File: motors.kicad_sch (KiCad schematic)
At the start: 15 parts, among them J5 left_motor_connector, J6 right_motor_connector, U2 L293D

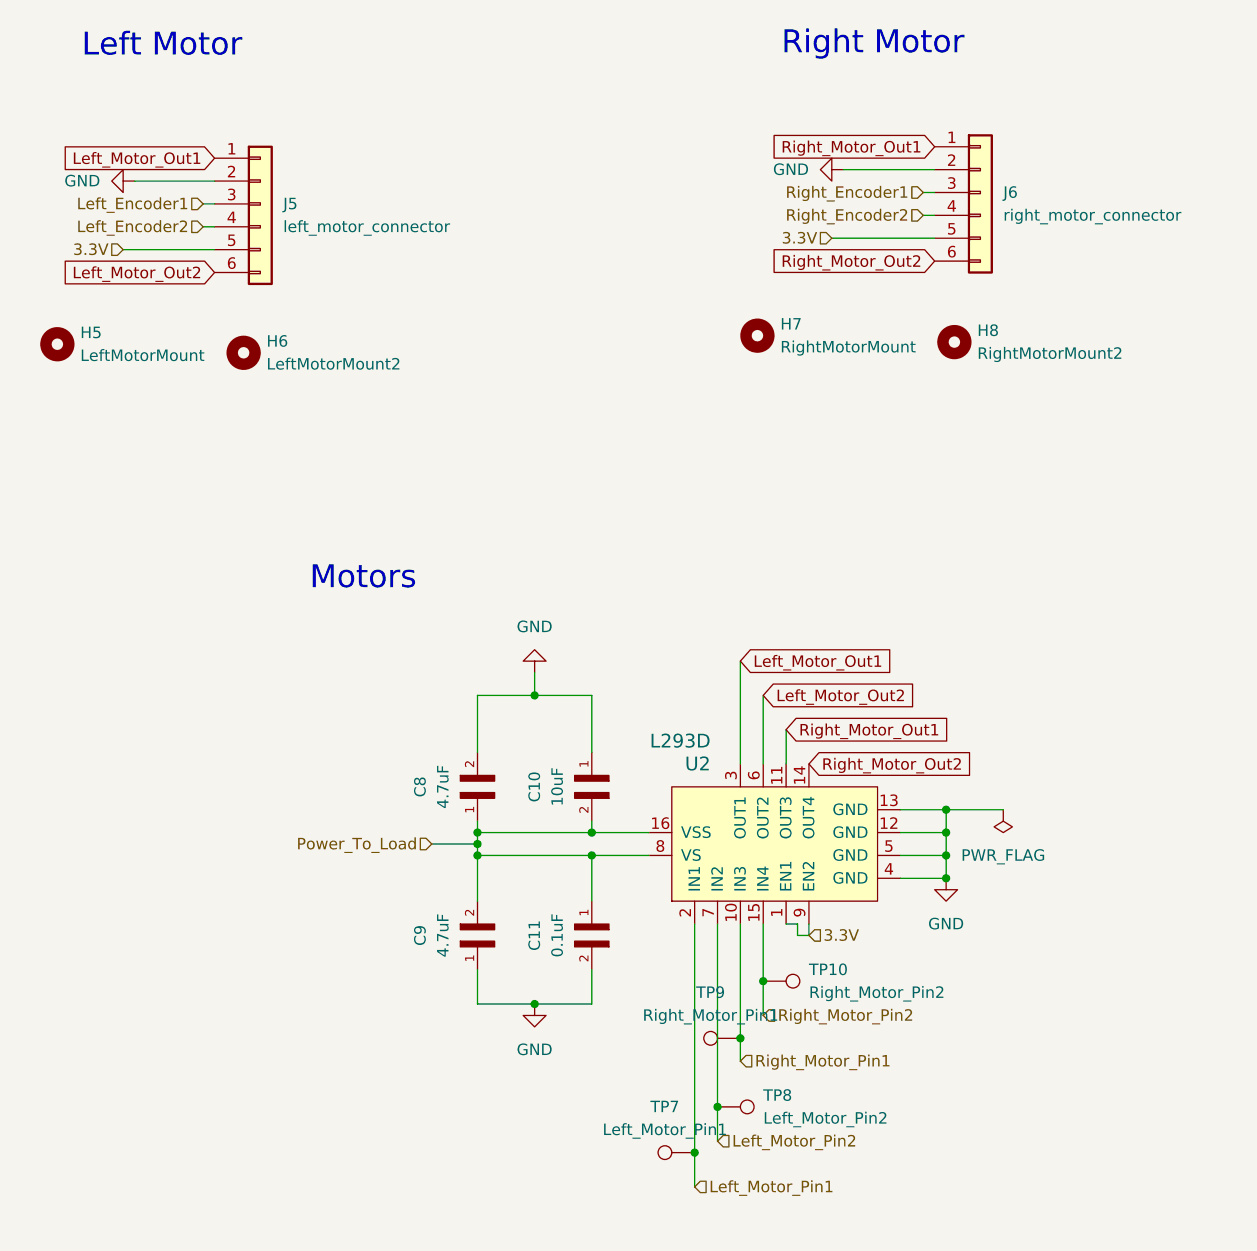
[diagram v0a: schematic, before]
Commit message: schematic: all errors and warnings gone
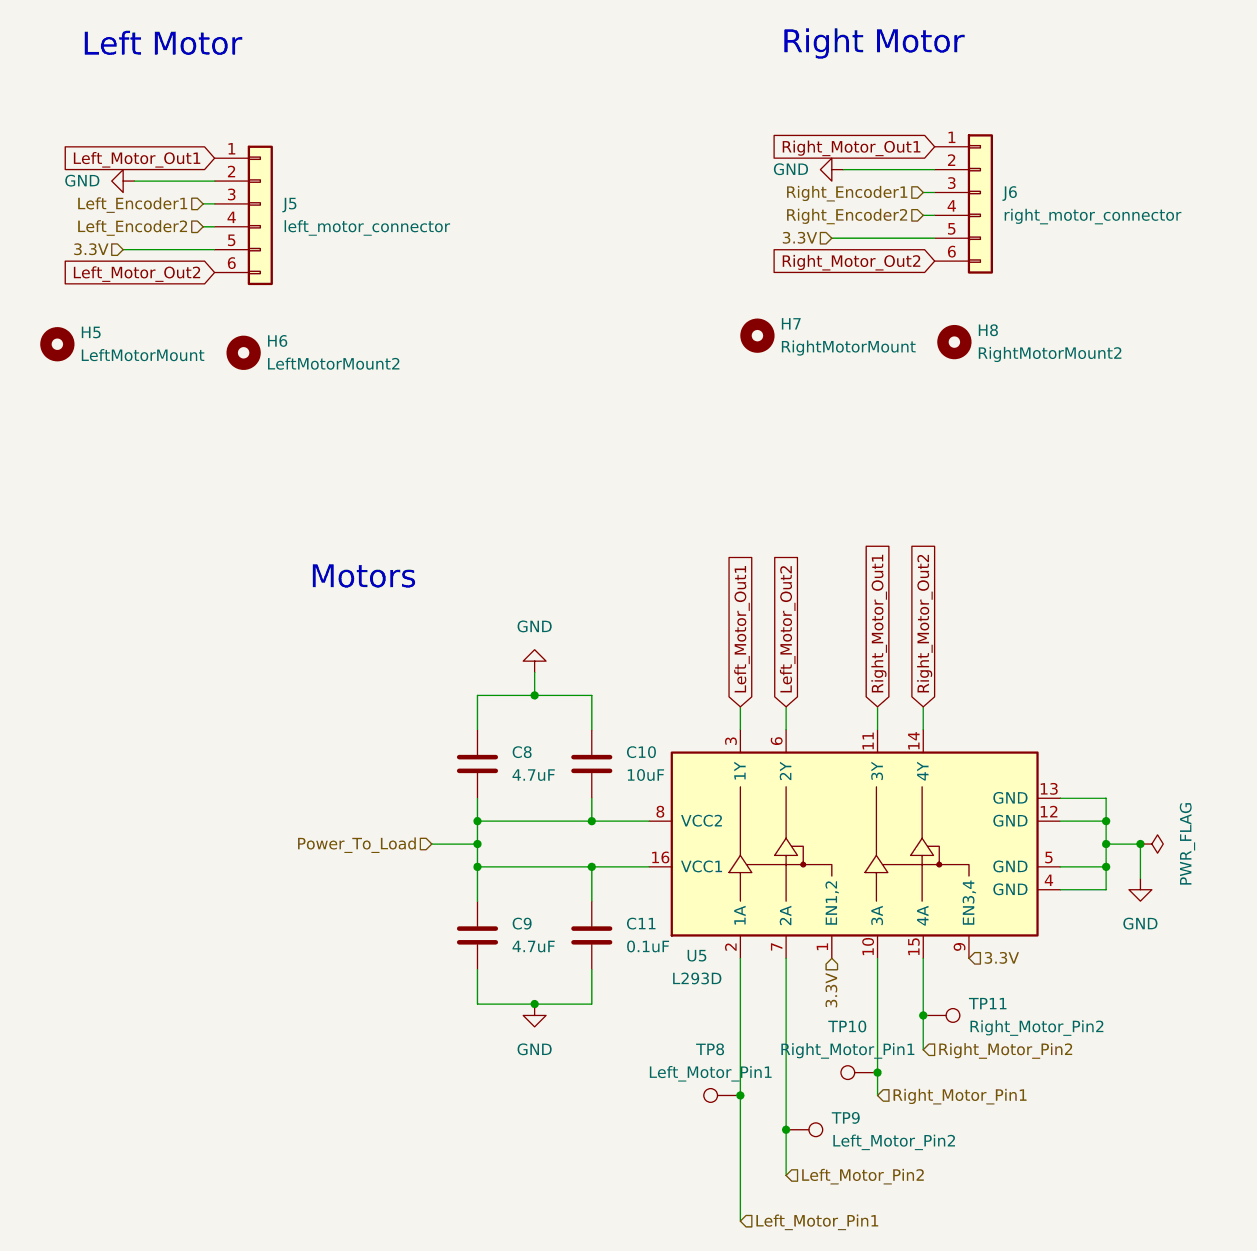
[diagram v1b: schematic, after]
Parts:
- removed C10: 10uF, Capacitor_SMD:C_0805_2012Metric_Pad1.18x1.45mm_HandSolder, symbol CL10A106KP8NNNC:CL10A106KP8NNNC
- removed C11: 0.1uF, Capacitor_SMD:C_0805_2012Metric_Pad1.18x1.45mm_HandSolder, symbol CL05B104KO5NNNC:CL05B104KO5NNNC
- removed C8, C9: 4.7uF, Capacitor_SMD:C_0805_2012Metric_Pad1.18x1.45mm_HandSolder, symbol CL10A475KO8NNNC:CL10A475KO8NNNC
- removed TP7: Left_Motor_Pin1, TestPoint:TestPoint_THTPad_2.0x2.0mm_Drill1.0mm, symbol Connector:TestPoint
- removed U2: L293D, Package_DIP:DIP-16_W7.62mm_Socket, symbol Robotastisch:L293D
- added C10: 10uF, Capacitor_SMD:C_0805_2012Metric_Pad1.18x1.45mm_HandSolder, symbol Device:C
- added C11: 0.1uF, Capacitor_SMD:C_0805_2012Metric_Pad1.18x1.45mm_HandSolder, symbol Device:C
- added C8, C9: 4.7uF, Capacitor_SMD:C_0805_2012Metric_Pad1.18x1.45mm_HandSolder, symbol Device:C
- added TP11: Right_Motor_Pin2, TestPoint:TestPoint_THTPad_2.0x2.0mm_Drill1.0mm, symbol Connector:TestPoint
- added U5: L293D, Package_DIP:DIP-16_W7.62mm, symbol Driver_Motor:L293D
- TP10: value Right_Motor_Pin2 -> Right_Motor_Pin1
- TP8: value Left_Motor_Pin2 -> Left_Motor_Pin1
- TP9: value Right_Motor_Pin1 -> Left_Motor_Pin2
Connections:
- net 3.3V: now also U5.1 (EN1,2), U5.9 (EN3,4)
- net GND: now also C10.1, C11.2, C8.1, C9.2, U5.12 (GND), U5.13 (GND), U5.4 (GND), U5.5 (GND)
- net Left_Motor_Out1: now also U5.3 (1Y)
- net Left_Motor_Out2: now also U5.6 (2Y)
- net Left_Motor_Pin1: now also TP8.1, U5.2 (1A)
- net Left_Motor_Pin2: now also TP9.1, U5.7 (2A); no longer TP8.1
- net Power_To_Load: now also C10.2, C11.1, C8.2, C9.1, U5.16 (VCC1), U5.8 (VCC2)
- net Right_Motor_Out1: now also U5.11 (3Y)
- net Right_Motor_Out2: now also U5.14 (4Y)
- net Right_Motor_Pin1: now also TP10.1, U5.10 (3A); no longer TP9.1
- net Right_Motor_Pin2: now also TP11.1, U5.15 (4A); no longer TP10.1

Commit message: pcb: all wired up, most warnings can't be fixed.
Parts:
- LM1: renamed from TP8; value Left_Motor_Pin1 -> Testpoint
- LM2: renamed from TP9; value Left_Motor_Pin2 -> Testpoint
- RM1: renamed from TP10; value Right_Motor_Pin1 -> Testpoint
- RM2: renamed from TP11; value Right_Motor_Pin2 -> Testpoint
- renumbered U5 to U2
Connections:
- net GND: now also C10.2, C8.2; no longer C10.1, C8.1
- net Power_To_Load: now also C10.1, C8.1; no longer C10.2, C8.2
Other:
- moved on the sheet: C10, C8
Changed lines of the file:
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@@
 		(dnp no)
 		(fields_autoplaced yes)
-		(property "Reference" "TP10"
+		(property "Reference" "RM1"
 			(at 117.348 140.97 90)
 			(effects
@@
 			)
 		)
-		(property "Value" "Right_Motor_Pin1"
+		(property "Value" "Testpoint"
 			(at 117.348 143.51 90)
 			(effects
@@
 			(project "RoboMaus"
 				(path "/0ec4df52-ef34-4d49-9154-02bae5c96110/599bc449-1c79-4d43-aa66-86532ca36330"
-					(reference "TP10")
+					(reference "RM1")
 					(unit 1)
 				)
@@
 	(symbol
 		(lib_id "Device:C")
-		(at 88.9 111.76 0)
+		(at 88.9 111.76 180)
 		(unit 1)
 		(exclude_from_sim no)
@@
 					(size 1.27 1.27)
 				)
-				(justify left)
+				(justify right)
 			)
 		)
@@
 					(size 1.27 1.27)
 				)
-				(justify left)
+				(justify right)
 			)
 		)
 		(property "Footprint" "Capacitor_SMD:C_0805_2012Metric_Pad1.18x1.45mm_HandSolder"
-			(at 89.8652 115.57 0)
+			(at 87.9348 107.95 0)
 			(effects
 				(font
@@
 		(dnp no)
 		(fields_autoplaced yes)
-		(property "Reference" "TP9"
+		(property "Reference" "LM2"
 			(at 115.57 151.1299 90)
 			(effects
@@
 			)
 		)
-		(property "Value" "Left_Motor_Pin2"
+		(property "Value" "Testpoint"
 			(at 115.57 153.6699 90)
 			(effects
@@
 			(project "RoboMaus"
 				(path "/0ec4df52-ef34-4d49-9154-02bae5c96110/599bc449-1c79-4d43-aa66-86532ca36330"
-					(reference "TP9")
+					(reference "LM2")
 					(unit 1)
 				)
@@
 	(symbol
 		(lib_id "Device:C")
-		(at 76.2 111.76 0)
+		(at 76.2 111.76 180)
 		(unit 1)
 		(exclude_from_sim no)
@@
 					(size 1.27 1.27)
 				)
-				(justify left)
+				(justify right)
 			)
 		)
@@
 					(size 1.27 1.27)
 				)
-				(justify left)
+				(justify right)
 			)
 		)
 		(property "Footprint" "Capacitor_SMD:C_0805_2012Metric_Pad1.18x1.45mm_HandSolder"
-			(at 77.1652 115.57 0)
+			(at 75.2348 107.95 0)
 			(effects
 				(font
@@
 		(dnp no)
 		(fields_autoplaced yes)
-		(property "Reference" "TP11"
+		(property "Reference" "RM2"
 			(at 130.81 138.4299 90)
 			(effects
@@
 			)
 		)
-		(property "Value" "Right_Motor_Pin2"
+		(property "Value" "Testpoint"
 			(at 130.81 140.9699 90)
 			(effects
@@
 			(project "RoboMaus"
 				(path "/0ec4df52-ef34-4d49-9154-02bae5c96110/599bc449-1c79-4d43-aa66-86532ca36330"
-					(reference "TP11")
+					(reference "RM2")
 					(unit 1)
 				)
@@
 		(dnp no)
 		(fields_autoplaced yes)
-		(property "Reference" "TP8"
+		(property "Reference" "LM1"
 			(at 102.108 143.51 90)
 			(effects
@@
 			)
 		)
-		(property "Value" "Left_Motor_Pin1"
+		(property "Value" "Testpoint"
 			(at 102.108 146.05 90)
 			(effects
@@
 			(project "RoboMaus"
 				(path "/0ec4df52-ef34-4d49-9154-02bae5c96110/599bc449-1c79-4d43-aa66-86532ca36330"
-					(reference "TP8")
+					(reference "LM1")
 					(unit 1)
 				)
@@
 		(on_board yes)
 		(dnp no)
-		(property "Reference" "U5"
+		(property "Reference" "U2"
 			(at 100.584 133.096 90)
 			(effects
@@
 			(project ""
 				(path "/0ec4df52-ef34-4d49-9154-02bae5c96110/599bc449-1c79-4d43-aa66-86532ca36330"
-					(reference "U5")
-					(unit 1)
-				)
+					(reference "U2")
+					(unit 1)
+				)
